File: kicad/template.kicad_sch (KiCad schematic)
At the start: 6 parts, among them J1 Bus_PCI_Express_x1, J6 USB_C_Receptacle_USB2.0_16P, U2 RP2040, U4 W25Q128JVP, U9 MCP25625T-E/ML, X1 ABM8-272-T3

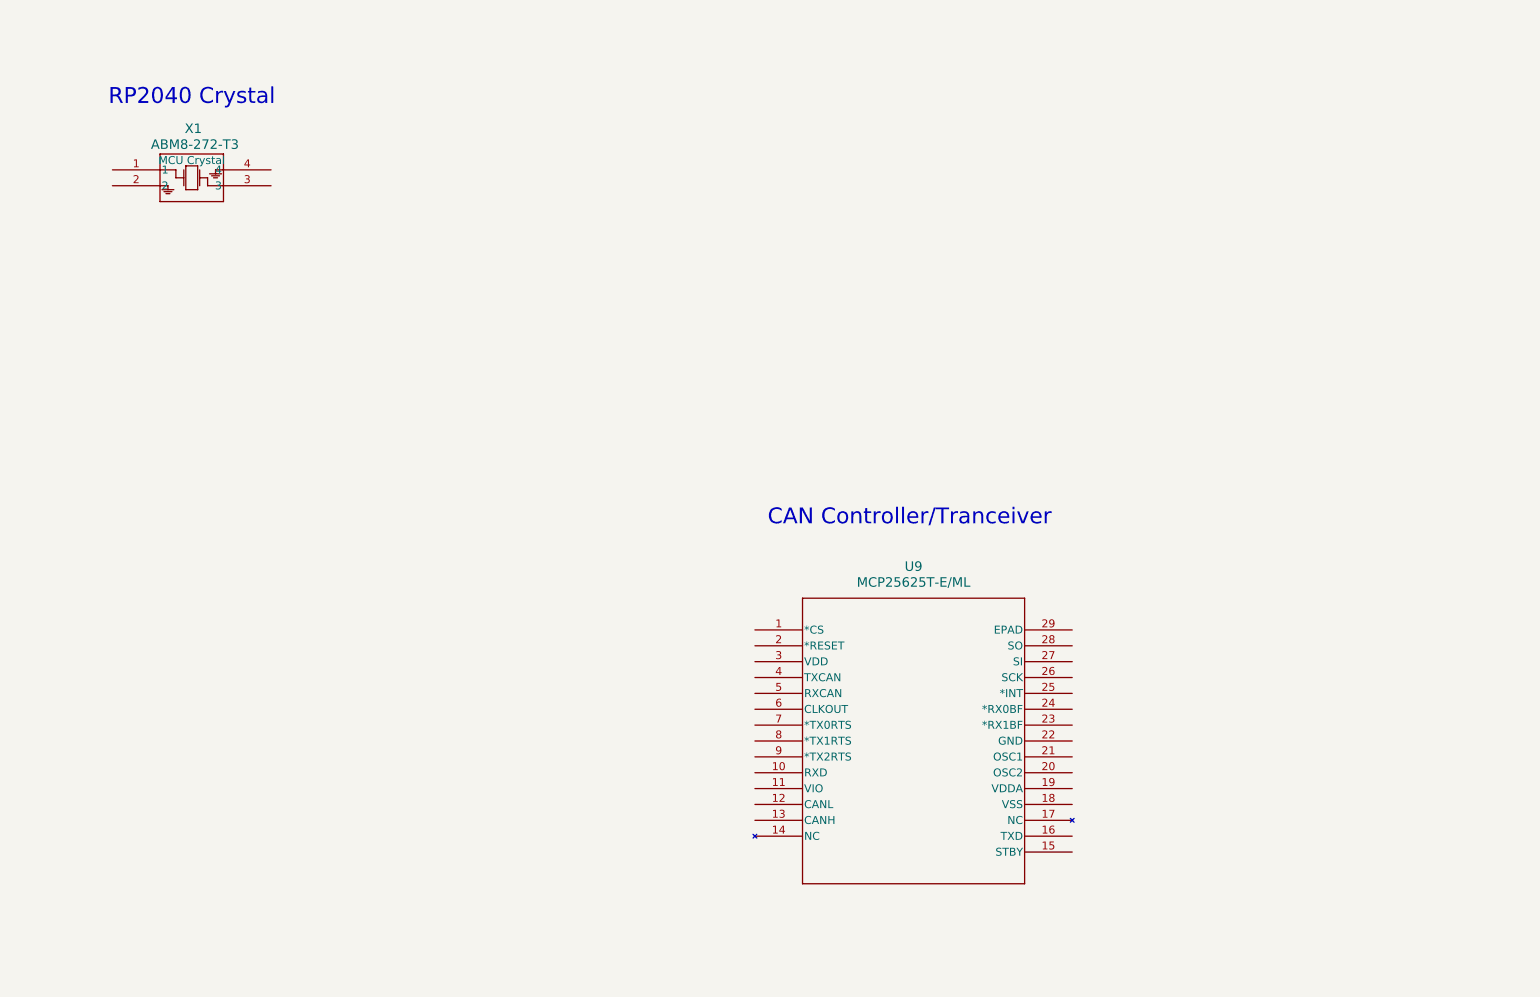
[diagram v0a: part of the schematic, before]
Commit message: refactor libraries
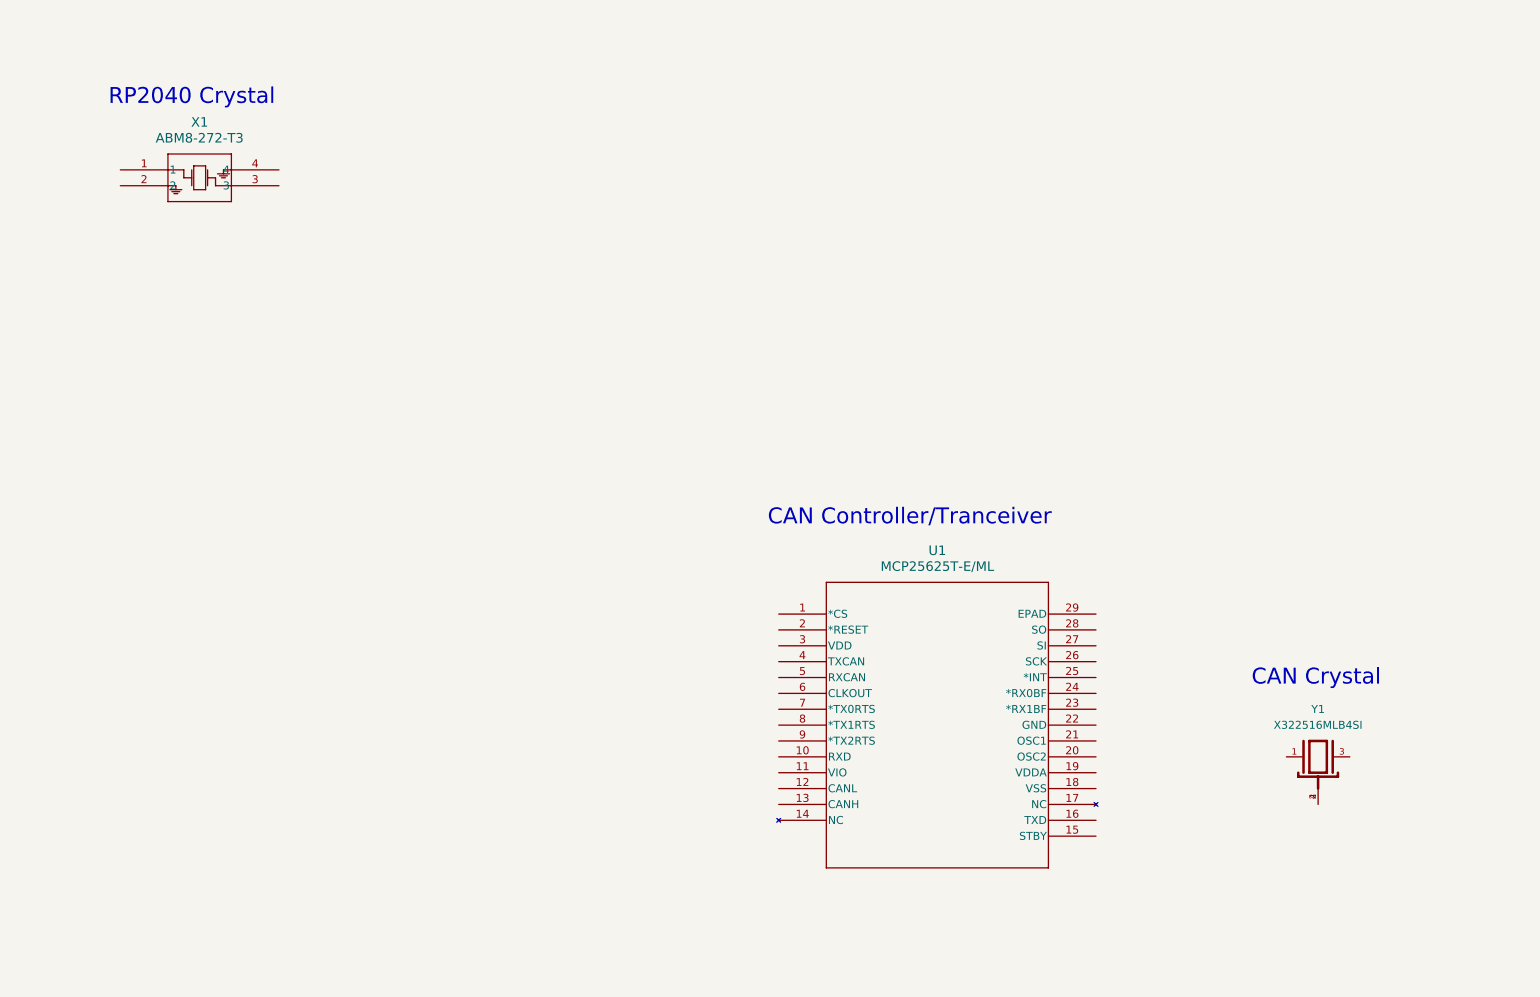
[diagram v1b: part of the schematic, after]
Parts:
- removed U9: MCP25625T-E/ML, MCP25625T_E_ML:QFN28_6X6MC_MCH, symbol MCP25625:MCP25625T-E_ML
- removed X1: ABM8-272-T3, ABM8-272-T3:ABM8-272-T3_ABR, symbol crystal:ABM8-272-T3
- added U1: MCP25625T-E/ML, challenge_template:QFN28_6X6MC_MCH, symbol challenge symbols:MCP25625T-E_ML
- added X1: ABM8-272-T3, challenge_template:ABM8-272-T3_ABR, symbol challenge symbols:ABM8-272-T3
- added Y1: X322516MLB4SI, challenge_template:OSC_X322516MLB4SI, symbol challenge symbols:X322516MLB4SI
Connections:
- new net: Y1.2, Y1.4
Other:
- note added: "CAN Crystal"
